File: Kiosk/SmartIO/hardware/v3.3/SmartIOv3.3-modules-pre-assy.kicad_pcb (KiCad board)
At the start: 2 copper layers, 353.8 x 196.1 mm, 66 parts, among them J1 LCD, J10 ADC, J11 TTL UART, J2 DB9, J3 MTN, J4 39910-0103, J6 ISP Hdr, J7 Keypad, J8 Scew terminals, K1 CB1aH-P-12V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

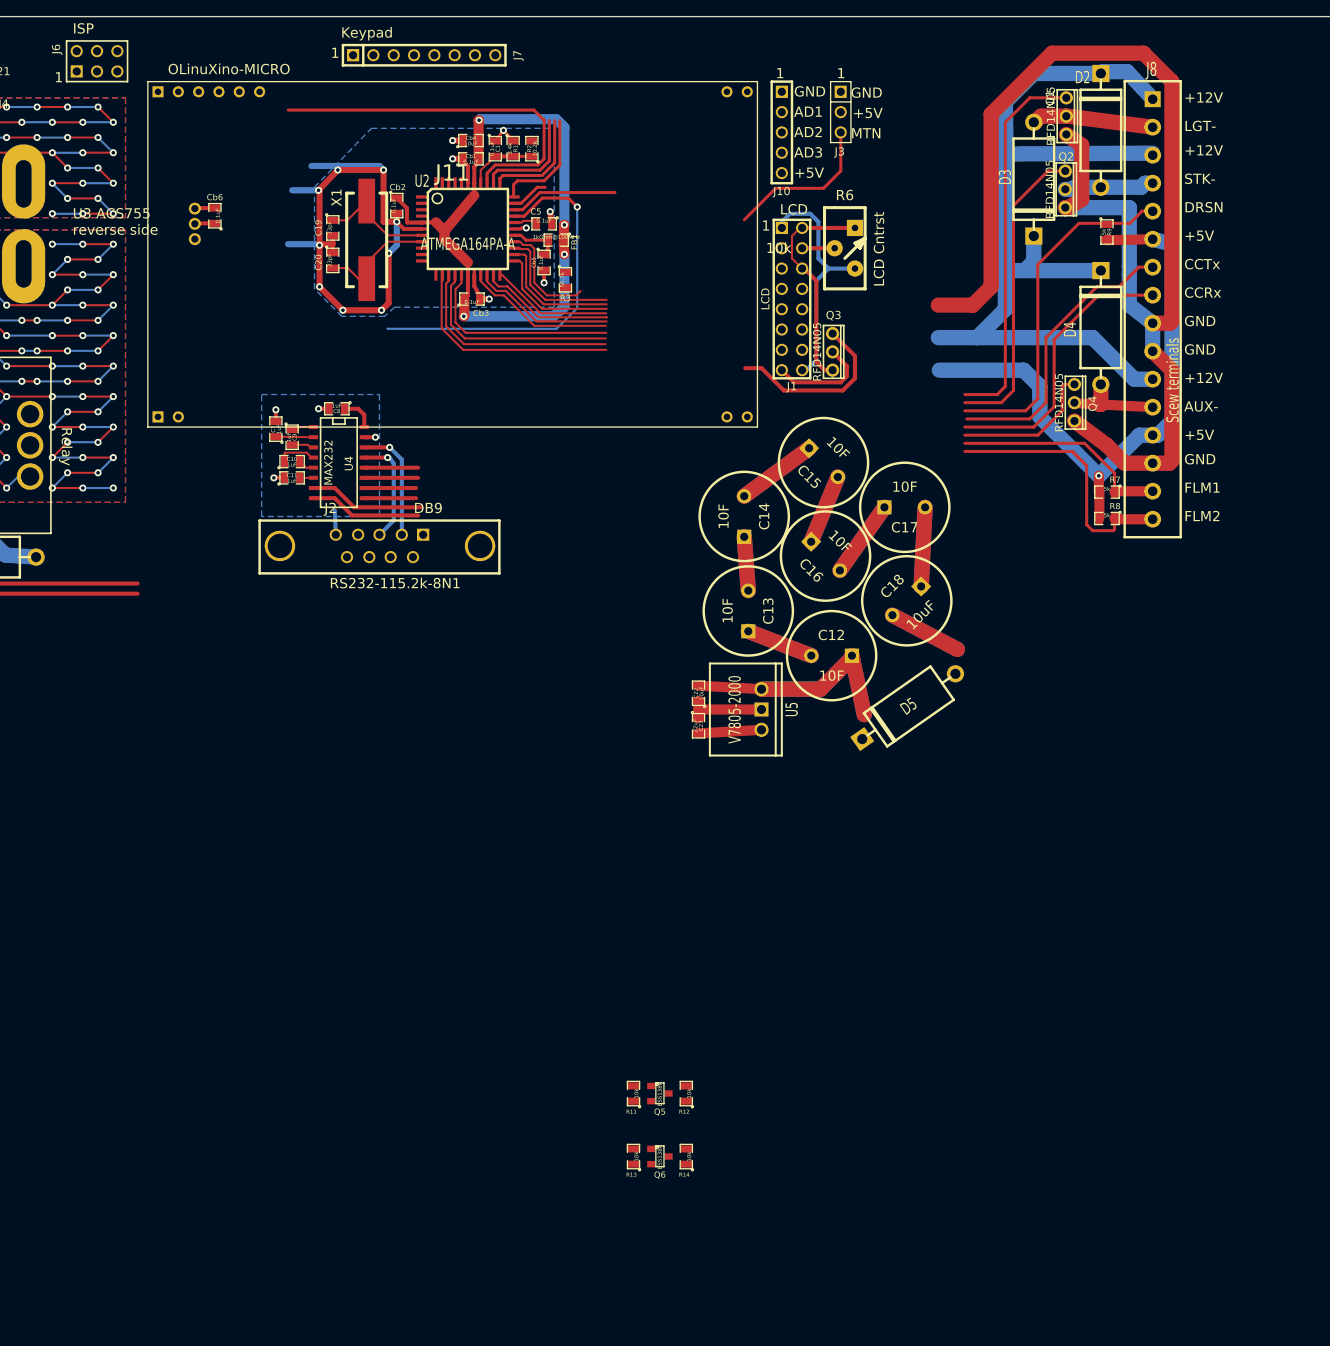
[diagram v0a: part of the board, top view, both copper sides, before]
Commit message: Added OLinuXino-MICRO header, made a pre-module-packing version of the board
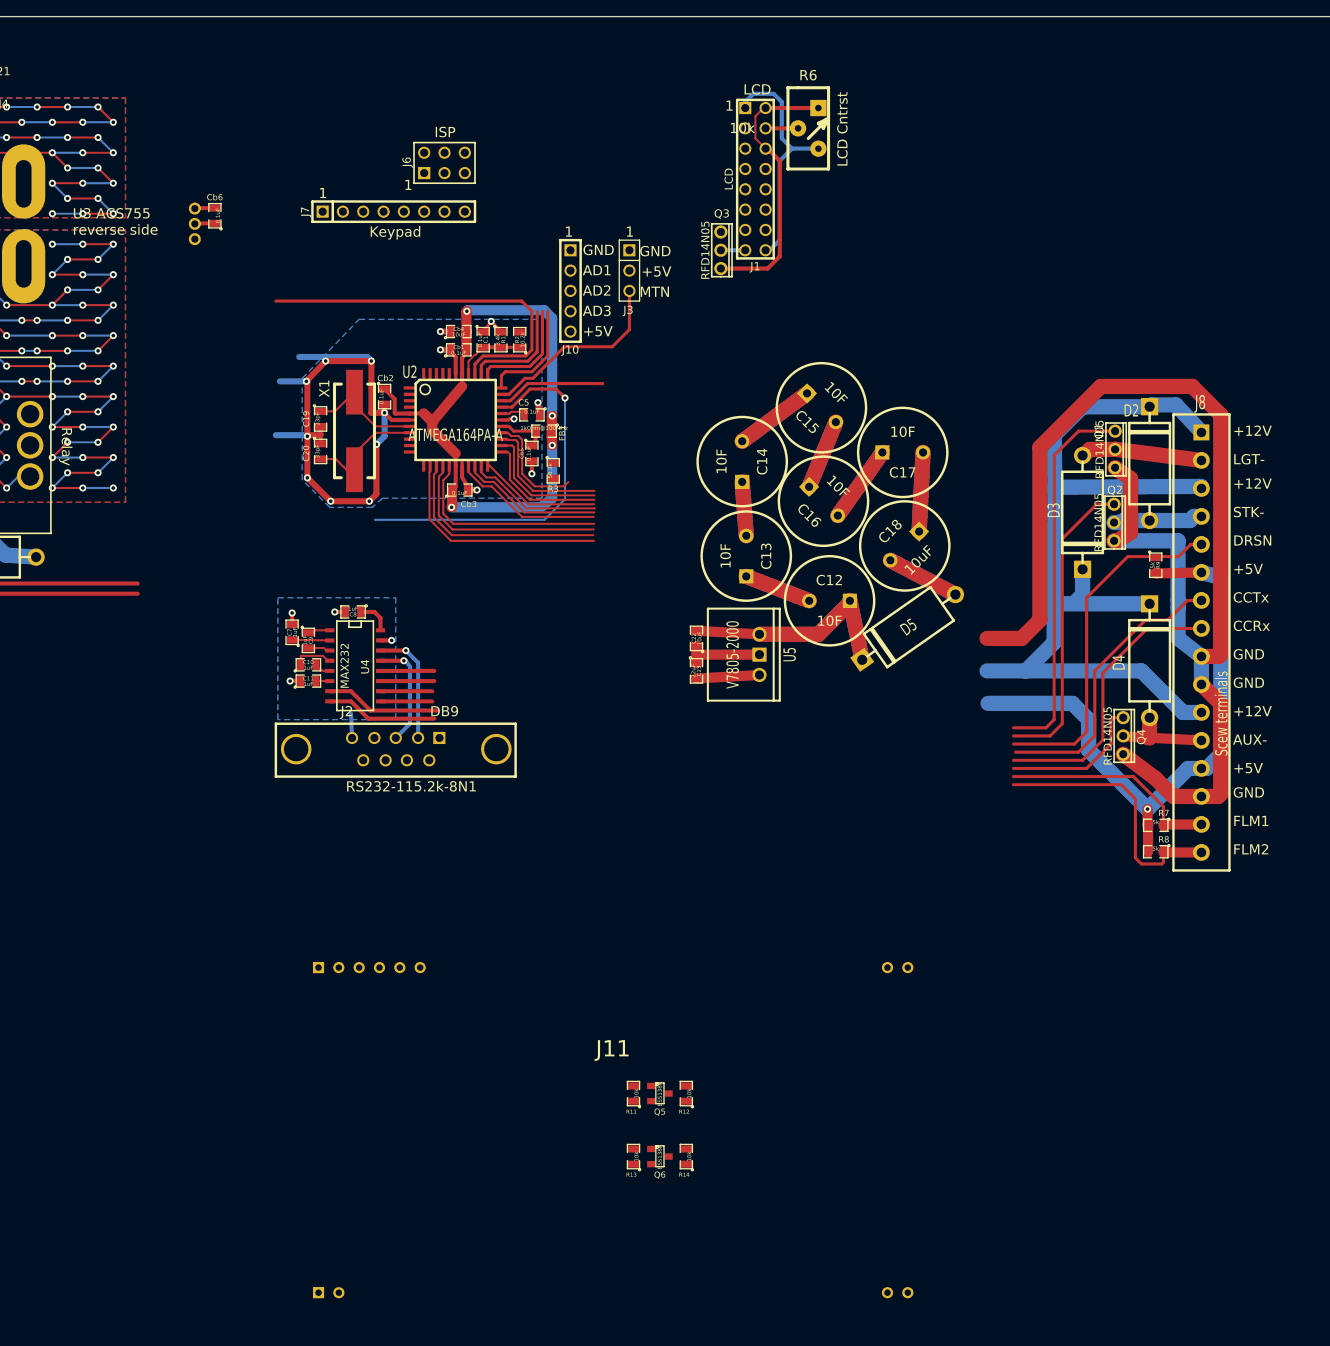
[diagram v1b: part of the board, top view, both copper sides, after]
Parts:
- moved J11 111.3 mm to (111.5, 151.9)
- moved J6 45.3 mm to (90.4, 31.0)
- moved D4 42.1 mm to (178.6, 93.2)
- moved Q1 42.1 mm to (174.2, 66.8)
- moved R7 42.1 mm to (179.3, 113.8)
- moved D2 42.1 mm to (178.6, 68.6)
- moved D3 42.1 mm to (170.2, 74.7)
- moved J8 42.1 mm to (185.0, 90.9)
- moved Q2 42.1 mm to (174.1, 75.9)
- moved Q4 42.1 mm to (175.3, 102.6)
- moved R9 42.1 mm to (179.3, 81.3)
- moved R8 42.1 mm to (179.3, 117.1)
- moved J3 33.0 mm to (113.5, 44.5)
- moved J10 33.0 mm to (106.2, 47.0)
- moved C10 25.5 mm to (73.4, 93.7)
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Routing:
- net PC6: track 39.0 -> 16.8 mm
- net LCDBL-: track 12.9 -> 3.05 mm
- net GND: track 321.4 -> 328.7 mm
